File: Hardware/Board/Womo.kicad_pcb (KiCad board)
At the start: 4 copper layers, 255 x 150 mm, 464 parts, among them IC1 SPSGRFC-868, IC200 BTS6143D, IC201 BTS6143D, IC203 BTS6143D, IC204 BTS6143D, J1 USB_B_Micro, J2 Conn_ARM_JTAG_SWD_20, J3 SD_Card, J300 734-264, J301 733-368, J302 733-368, J303 733-368, J304 Truma, J305 Dormetic, J306 733-366, J307 733-366, J308 733-366, J309 733-366, J310 733-370, J311 734-163, J312 734-163, J313 734-163, J314 734-163, J315 734-168, J316 733-363, J317 RJ45_Shielded, J318 Spare, J319 SENSOR, J320 Raspberry_Pi_2_3, J321 Wasser, J322 Abwasser, J323 733-370, J324 Waveshare IoT Hat, J325 734-168, J326 733-366, J400 USB_B_Micro, J401 RJ45_Shielded, J500 SENSOR, K300 5-1393243-2, K301 5-1393243-2, K302 5-1393243-2, K303 5-1393243-2, Q100 2N7002, Q102 2N7002, Q103 2N7002, Q104 2N7002, Q200 2N7002, Q201 2N7002, Q202 2N7002, Q203 2N7002, SW1 Boot, SW3 Reset, U1 STM32L476ZGTx, U100 MAX17572, U101 MAX17572, U102 MAX17572, U104 MAX17574, U105 MAX17574, U2 M25Q128A, U200 SN74LV4052A, U201 TJA1029T, U202 TJA1029T, U203 TJA1029T, U204 TJA1029T, U205 SN74LV4052A, U206 SN74LV4052A, U207 MAX3072E, U208 MAX3072E, U209 MAX3072E, U210 MAX3072E, U211 MAX11615, U212 PCF8574A, U213 TJA1049T-3, U214 DS2482S-800+, U215 SN74LV4052A, U216 Si8642BB-B-IS1, U217 Si8642BB-B-IS1, U3 24AA02UID, U300 max4896atp+, U301 max4896atp+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

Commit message: Daten für Vortrag 36c3 ergänzt
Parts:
- moved J2 8.02 mm to (348.0, 169.5)
- moved R231 5.16 mm to (207.5, 141.2)
- moved R230 3.88 mm to (213.7, 141.2)
- moved FB212 2.45 mm to (211.7, 137.9)
- moved FB213 2.33 mm to (209.3, 137.9)
- moved D216 2.26 mm to (210.6, 141.5)
- moved C219 2.20 mm to (210.7, 145.1)
- moved C227 0.87 mm to (163.6, 244.4)
- moved J317 0.83 mm to (365.9, 266.8)
- moved J310 0.79 mm to (304.3, 266.4)
- moved J304 0.65 mm to (332.7, 142.1)
- moved J305 0.64 mm to (318.5, 139.3)
- moved J307 0.64 mm to (231.3, 133.5)
- moved J316 0.64 mm to (211.7, 133.5)
- moved J326 0.63 mm to (376.0, 133.5)
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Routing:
- net Net-(D218-Pad5): track 0.00 -> 21.6 mm
- net K4_NC: track 0.00 -> 18.7 mm
- net K2_NC: track 0.00 -> 17.7 mm
- net K3_NC: track 0.00 -> 17.7 mm
- net K1_NC: track 0.00 -> 17.7 mm
- net Net-(D216-Pad2): track 0.00 -> 16.0 mm, vias 0 -> 2
- net K2_COM: track 0.00 -> 15.8 mm
- net K3_COM: track 0.00 -> 15.7 mm
- net K1_COM: track 0.00 -> 15.3 mm
- net K4_COM: track 0.00 -> 15.0 mm
- net Net-(D216-Pad1): track 0.00 -> 12.9 mm
- net K1_NO: track 0.00 -> 12.2 mm
- net K2_NO: track 0.00 -> 10.8 mm
- net K3_NO: track 0.00 -> 10.8 mm
- net K4_NO: track 0.00 -> 10.5 mm
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- added copper zone on B.Cu, net DC_Input
- added copper zone on F.Cu, net HSS_1
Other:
- net class Medium added: clearance 0.2, trace_width 0.3, via_dia 0.8, via_drill 0.4
- net class Power_high added: clearance 0.2, trace_width 1.5, via_dia 0.8, via_drill 0.4
- net class Power_smal added: clearance 0.2, trace_width 0.5, via_dia 0.8, via_drill 0.4

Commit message: Kleinkram Layout
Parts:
- moved C221 5.02 mm to (177.3, 152.8)
- moved R310 4.92 mm to (346.8, 252.3), turned to 0 degrees
- moved R313 4.91 mm to (353.3, 252.3), turned to 180 degrees
- moved R312 3.34 mm to (351.6, 250.7), turned to 0 degrees
- moved R311 3.32 mm to (348.4, 250.7), turned to 180 degrees
- moved R317 3.03 mm to (354.1, 254.7)
- moved R315 2.82 mm to (349.1, 254.7)
- moved R316 2.80 mm to (350.8, 254.7)
- moved C325 2.69 mm to (346.8, 262.3), turned to 0 degrees
- moved R314 2.55 mm to (346.0, 254.7)
- moved C328 2.27 mm to (353.3, 262.3), turned to 180 degrees
- moved FB342 2.17 mm to (350.8, 257.9)
- moved FB341 2.15 mm to (349.1, 257.9)
- moved FB343 2.15 mm to (354.1, 257.9)
- moved FB340 2.12 mm to (346.0, 257.9)
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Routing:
- net GND: track 2.92 -> 86.1 mm, vias 15 -> 24
- net +3.3VA: track 0.00 -> 66.7 mm, vias 0 -> 6
- net Net-(D218-Pad1): track 1.75 -> 32.5 mm, vias 0 -> 2
- net Net-(D218-Pad3): track 1.74 -> 27.2 mm
- net Net-(D217-Pad1): track 1.71 -> 24.6 mm, vias 0 -> 3
- net Net-(D217-Pad5): track 1.74 -> 24.4 mm
- net Net-(D217-Pad4): track 1.74 -> 18.1 mm, vias 0 -> 2
- net Net-(D217-Pad3): track 1.74 -> 17.1 mm, vias 0 -> 2
- net Net-(C219-Pad1): track 0.00 -> 14.5 mm, vias 0 -> 2
- net Net-(D218-Pad4): track 8.57 -> 19.0 mm, vias 0 -> 2
- net Net-(C326-Pad1): track 0.00 -> 8.00 mm
- net Net-(C328-Pad1): track 0.00 -> 7.98 mm
- net Net-(C327-Pad1): track 0.00 -> 7.82 mm
- net Net-(C325-Pad1): track 0.00 -> 7.75 mm
- net AIN5: track 0.00 -> 3.26 mm
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
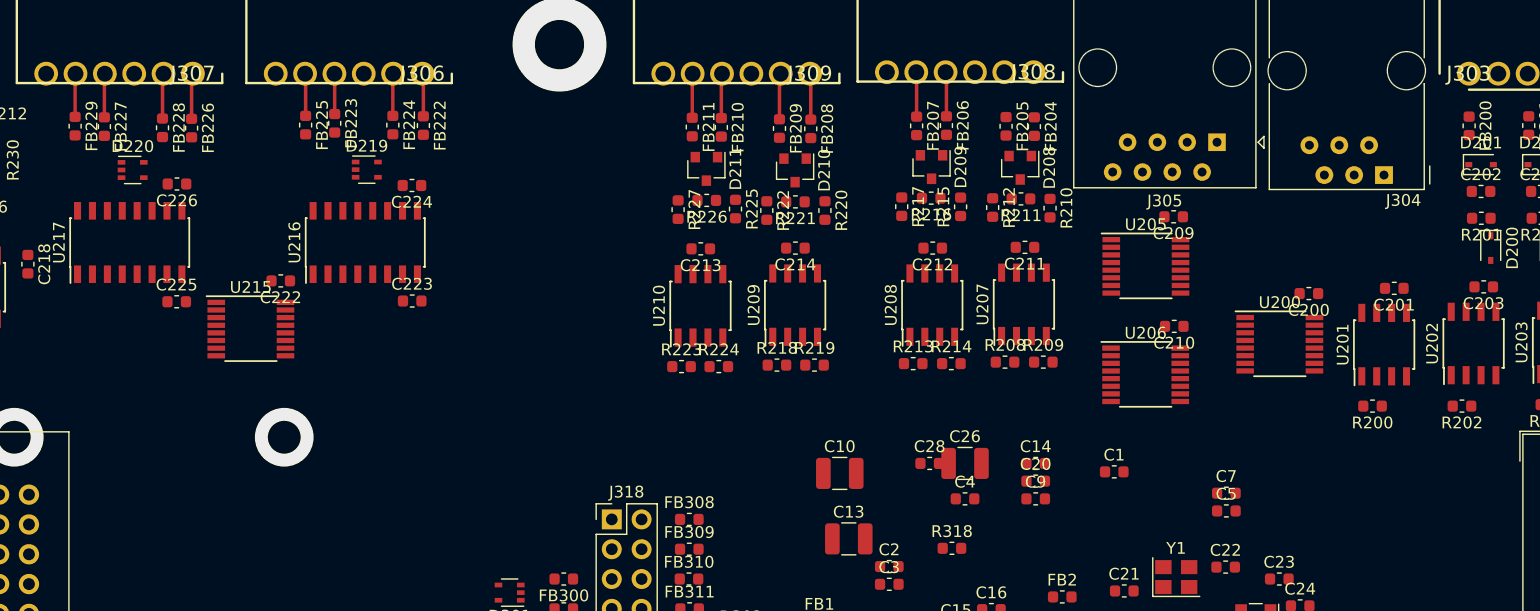
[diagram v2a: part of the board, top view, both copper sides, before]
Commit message: Layout Arbeit, Project Library sollte jetzt auf allen Rechnern funktionieren. Leerzeichen entfernt.
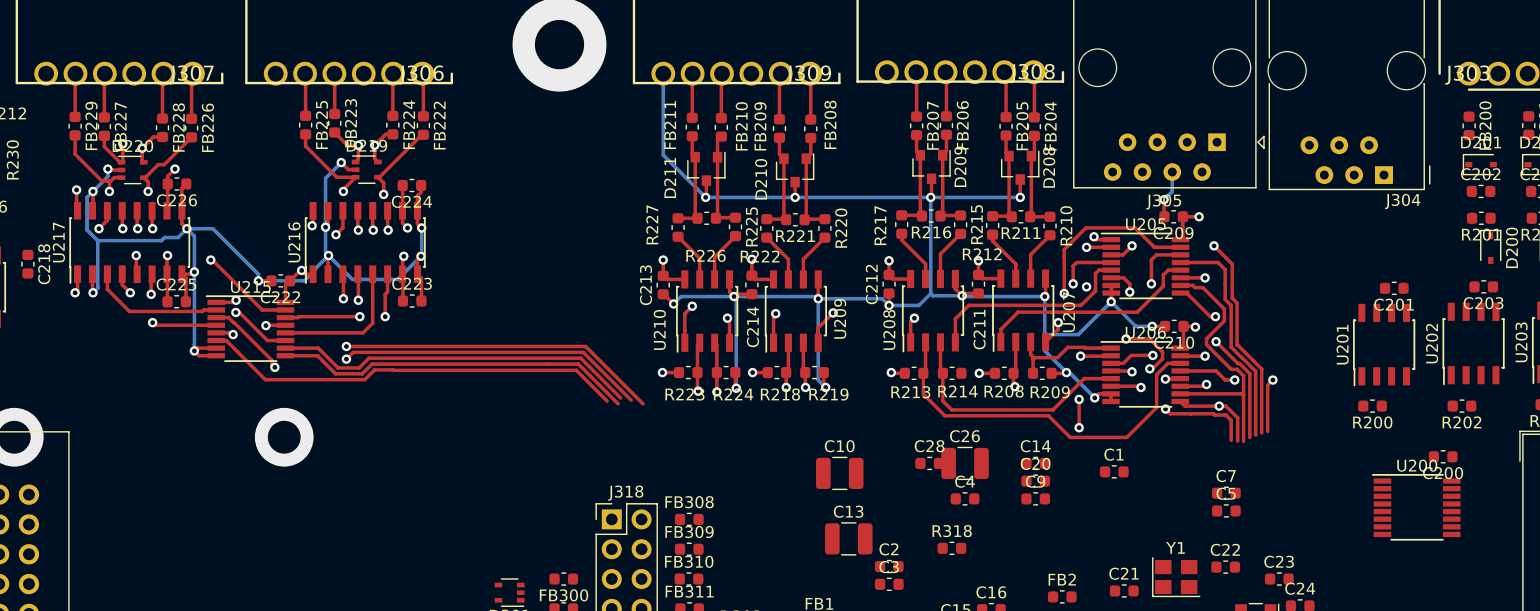
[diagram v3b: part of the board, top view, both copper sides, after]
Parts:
- moved U200 18.2 mm to (335.6, 170.5)
- moved C200 18.0 mm to (337.8, 166.1)
- moved C211 5.05 mm to (298.2, 151.4), turned to 90 degrees
- moved C214 4.86 mm to (278.9, 151.5), turned to 90 degrees
- moved C212 4.83 mm to (290.6, 151.4), turned to 90 degrees
- moved C213 4.45 mm to (271.3, 151.5), turned to 90 degrees
- moved R210 1.52 mm to (304.3, 146.5)
- moved R211 1.52 mm to (301.8, 145.7)
- moved R212 1.52 mm to (299.4, 146.4)
- moved R215 1.52 mm to (296.7, 146.3), turned to 270 degrees
- moved R216 1.52 mm to (294.2, 145.6)
- moved R217 1.52 mm to (291.7, 146.3)
- moved R220 1.52 mm to (285.1, 146.7)
- moved R221 1.52 mm to (282.6, 145.9)
- moved R222 1.52 mm to (280.2, 146.7)
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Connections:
- FB222 pad 2: Net-(D219-Pad1) -> Net-(D219-Pad4)
- FB223 pad 2: Net-(D219-Pad3) -> Net-(D219-Pad1)
- FB224 pad 2: Net-(D219-Pad4) -> Net-(D219-Pad5)
- FB225 pad 2: Net-(D219-Pad5) -> Net-(D219-Pad3)
- FB226 pad 2: Net-(D220-Pad1) -> Net-(D220-Pad4)
- FB227 pad 2: Net-(D220-Pad3) -> Net-(D220-Pad1)
- FB228 pad 2: Net-(D220-Pad4) -> Net-(D220-Pad5)
- FB229 pad 2: Net-(D220-Pad5) -> Net-(D220-Pad3)
- U205 pad 15: RX_RS485_2 -> RX_RS485_3
- U205 pad 3: LPUART3_TX_RS485 -> LPUART_TX_RS485
- U206 pad 1: TX_RS485_1 -> DE_RS485_1
- U206 pad 2: TX_RS485_3 -> DE_RS485_3
- U206 pad 4: TX_RS485_4 -> DE_RS485_4
- U206 pad 5: TX_RS485_2 -> DE_RS485_2
- U216 pad 11: Net-(D219-Pad5) -> Net-(D219-Pad3)
- U216 pad 12: Net-(D219-Pad4) -> Net-(D219-Pad5)
- U216 pad 13: Net-(D219-Pad3) -> Net-(D219-Pad1)
- U216 pad 14: Net-(D219-Pad1) -> Net-(D219-Pad4)
- U217 pad 11: Net-(D220-Pad5) -> Net-(D220-Pad3)
- U217 pad 12: Net-(D220-Pad4) -> Net-(D220-Pad5)
- U217 pad 13: Net-(D220-Pad3) -> Net-(D220-Pad1)
- U217 pad 14: Net-(D220-Pad1) -> Net-(D220-Pad4)
- U217 pad 4: TX_SER4 -> TX_SER_4
- U217 pad 5: RX_SER3 -> RX_SER_3
- U217 pad 6: RX_SER4 -> RX_SER_4
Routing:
- net +3.3VA: track 66.7 -> 319.8 mm, vias 6 -> 24
- net GND: track 86.1 -> 329.9 mm, vias 24 -> 53
- net RE_RS485_4: track 0.00 -> 52.0 mm, vias 0 -> 2
- net RX_RS485_4: track 0.00 -> 50.5 mm, vias 0 -> 2
- net RE_RS485_3: track 0.00 -> 50.5 mm, vias 0 -> 4
- net DE_RS485_4: track 0.00 -> 45.4 mm, vias 0 -> 2
- net RX_RS485_3: track 0.00 -> 44.2 mm, vias 0 -> 2
- net USART3_TX_SER: track 0.00 -> 39.5 mm, vias 0 -> 2
- net TX_RS485_4: track 0.00 -> 38.0 mm, vias 0 -> 2
- net USART3_RX_SER: track 0.00 -> 36.6 mm, vias 0 -> 2
- net SER_SEL_EN: track 0.00 -> 36.1 mm
- net DE_RS485_3: track 0.00 -> 33.2 mm, vias 0 -> 2
- net RE_RS485_2: track 0.00 -> 32.2 mm
- net TX_RS485_3: track 0.00 -> 31.4 mm, vias 0 -> 3
- net SER_SEL_A0: track 0.00 -> 31.0 mm
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
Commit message: Zwischenstand Layout, etliche Fehler im Schaltplan gefixt.
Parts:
- added D307: SP0504BAJT, Package_TO_SOT_SMD:SOT-353_SC-70-5, F.Cu at (367.7, 143.0)
- moved C305 118.1 mm to (339.0, 222.5), turned to 180 degrees
- moved U302 106.6 mm to (331.4, 227.6), turned to 270 degrees
- moved C304 97.9 mm to (327.6, 231.3), turned to 270 degrees
- moved C316 92.7 mm to (343.1, 231.4), turned to 270 degrees
- moved IC1 86.1 mm to (251.8, 208.6)
- moved U304 82.0 mm to (346.9, 227.6), turned to 270 degrees
- moved C317 80.7 mm to (346.9, 222.6), turned to 180 degrees
- moved R318 64.5 mm to (263.2, 229.5), turned to 90 degrees
- moved C29 47.9 mm to (331.3, 222.5), turned to 180 degrees
- moved C31 42.8 mm to (335.3, 231.2), turned to 270 degrees
- moved Q203 35.0 mm to (194.4, 233.7), turned to 270 degrees
- moved U6 33.9 mm to (339.1, 227.6)
- moved R250 31.3 mm to (195.4, 230.2), turned to 90 degrees
- moved R252 29.6 mm to (193.5, 230.2), turned to 270 degrees
- moved D305 25.8 mm to (285.1, 239.1), turned to 180 degrees
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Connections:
- C202 pad 1: Net-(C202-Pad1) -> LIN1
- C204 pad 1: Net-(C204-Pad1) -> LIN2
- C206 pad 1: Net-(C206-Pad1) -> LIN3
- C208 pad 1: Net-(C208-Pad1) -> LIN4
- D201 pad 1: Net-(C202-Pad1) -> Net-(D201-Pad1)
- D203 pad 1: Net-(C204-Pad1) -> Net-(D203-Pad1)
- D205 pad 1: Net-(C206-Pad1) -> Net-(D205-Pad1)
- D207 pad 1: Net-(C208-Pad1) -> Net-(D207-Pad1)
- D305 pad 3: I2C1_SDA -> Net-(D305-Pad3)
- D305 pad 4: I2C1_SCL -> Net-(D305-Pad4)
- D305 pad 5: +3.3VA -> Net-(D305-Pad5)
- FB200 pad 2: Net-(C202-Pad1) -> Net-(D201-Pad1)
- FB201 pad 2: Net-(C204-Pad1) -> Net-(D203-Pad1)
- FB202 pad 2: Net-(C206-Pad1) -> Net-(D205-Pad1)
- FB203 pad 2: Net-(C208-Pad1) -> Net-(D207-Pad1)
- J311 pad 1: K1_COM -> K1_NO
- J311 pad 2: K1_NC -> K1_COM
- J311 pad 3: K1_NO -> K1_NC
- J312 pad 1: K2_COM -> K2_NO
- J312 pad 2: K2_NC -> K2_COM
- J312 pad 3: K2_NO -> K2_NC
- J313 pad 1: K3_COM -> K3_NO
- J313 pad 2: K3_NC -> K3_COM
- J313 pad 3: K3_NO -> K3_NC
- J314 pad 1: K4_COM -> K4_NO
- J314 pad 2: K4_NC -> K4_COM
- J314 pad 3: K4_NO -> K4_NC
- R201 pad 2: Net-(C202-Pad1) -> Net-(D201-Pad1)
- R203 pad 2: Net-(C204-Pad1) -> Net-(D203-Pad1)
- R205 pad 2: Net-(C206-Pad1) -> Net-(D205-Pad1)
- R207 pad 2: Net-(C208-Pad1) -> Net-(D207-Pad1)
- U200 pad 13: UART4_RX_LIN -> USART2_RX_LIN
- U200 pad 3: UART4_TX_LIN -> USART2_TX_LIN
- U201 pad 6: Net-(C202-Pad1) -> Net-(D201-Pad1)
- U202 pad 6: Net-(C204-Pad1) -> Net-(D203-Pad1)
- U203 pad 6: Net-(C206-Pad1) -> Net-(D205-Pad1)
- U204 pad 6: Net-(C208-Pad1) -> Net-(D207-Pad1)
- U205 pad 3: LPUART_TX_RS485 -> LPUART3_TX_RS485
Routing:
- net GND: track 329.9 -> 943.7 mm, vias 53 -> 99
- net I2C2_SCL: track 0.00 -> 99.4 mm
- net I2C2_SDA: track 0.00 -> 98.4 mm
- net HSS_1_EN: track 0.00 -> 83.7 mm
- net HSS_2_EN: track 0.00 -> 80.0 mm
- net +5V: track 0.00 -> 78.3 mm, vias 0 -> 1
- net HSS_3_EN: track 0.00 -> 78.1 mm
- net K1_STATUS: track 0.00 -> 76.9 mm, vias 0 -> 1
- net HSS_4_EN: track 0.00 -> 73.7 mm
- net +3V3: track 0.00 -> 69.1 mm, vias 0 -> 5
- net +3.3VA: track 319.8 -> 388.5 mm, vias 24 -> 29
- net K2_STATUS: track 0.00 -> 65.4 mm, vias 0 -> 1
- net K1_RESET: track 0.00 -> 65.0 mm, vias 0 -> 2
- net I2C1_SDA: track 0.00 -> 61.4 mm
- net STB-CAN: track 0.00 -> 61.1 mm
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
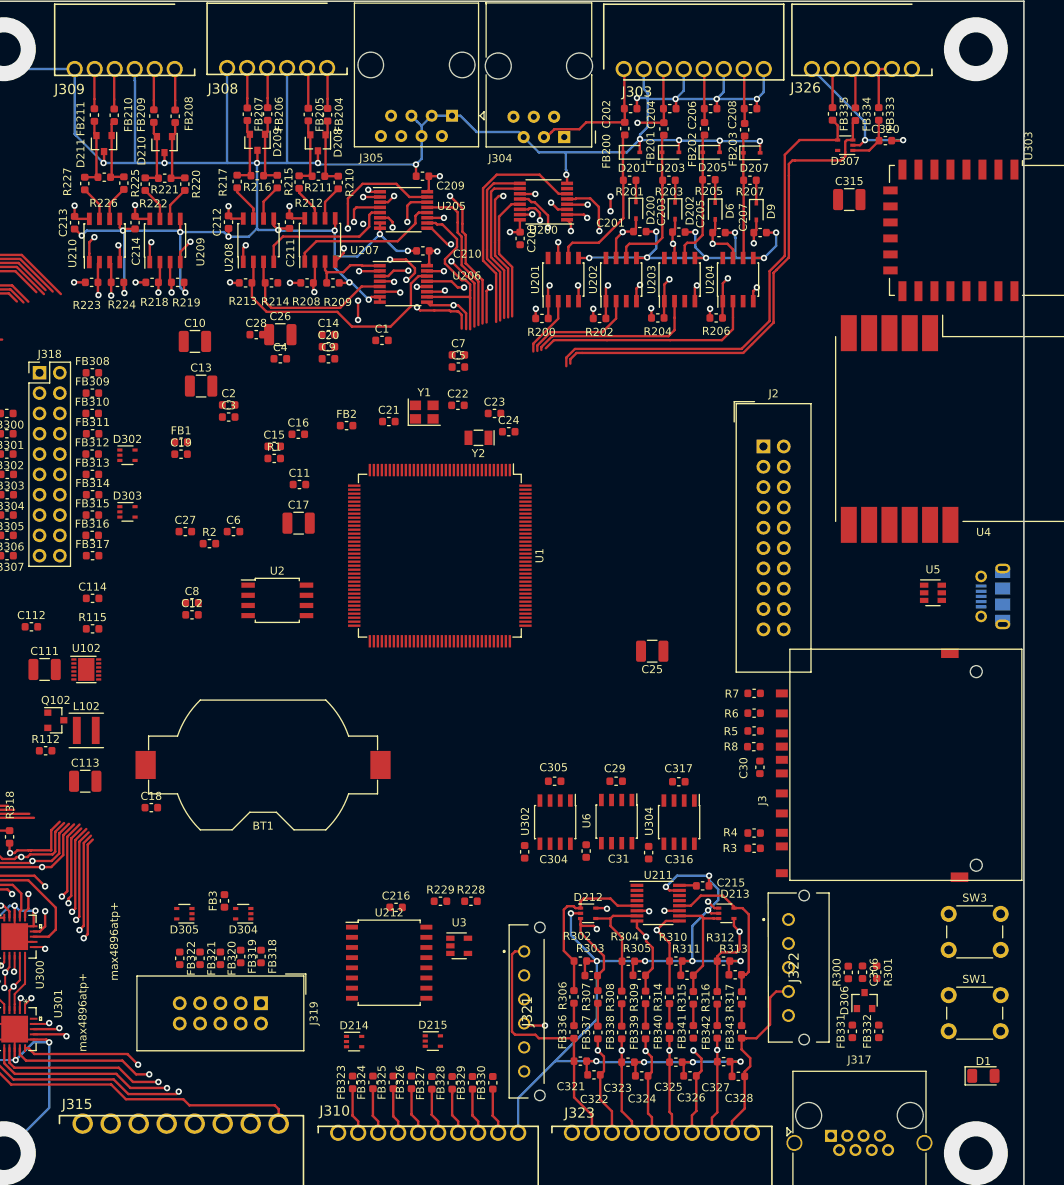
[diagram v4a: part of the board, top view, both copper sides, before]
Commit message: Fehlende Masse Abblockung CPU, Anfang Prozessor Routing
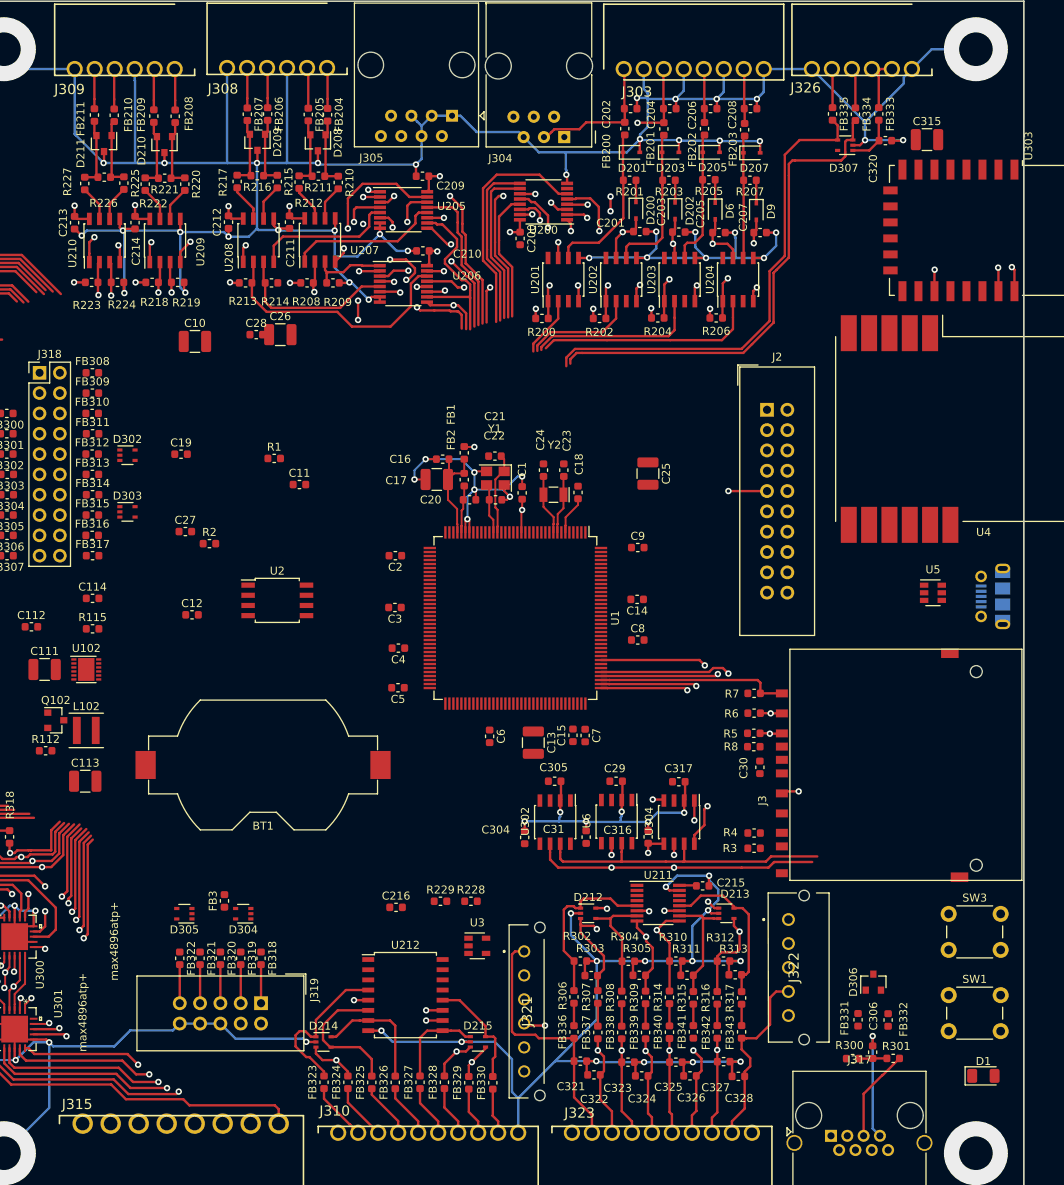
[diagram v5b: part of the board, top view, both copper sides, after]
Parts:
- moved C18 66.3 mm to (334.3, 186.4), turned to 90 degrees
- moved C13 60.9 mm to (328.7, 217.7), turned to 270 degrees
- moved C8 55.9 mm to (341.7, 204.9)
- moved C15 52.0 mm to (333.6, 216.8), turned to 90 degrees
- moved C14 50.8 mm to (341.7, 199.8), turned to 180 degrees
- moved C7 50.1 mm to (335.2, 216.8), turned to 270 degrees
- moved C9 45.3 mm to (341.7, 193.3)
- moved C6 41.0 mm to (323.2, 216.9), turned to 270 degrees
- moved C5 40.8 mm to (311.8, 210.8), turned to 180 degrees
- moved C4 39.1 mm to (311.8, 205.9), turned to 180 degrees
- moved FB1 35.7 mm to (320.0, 184.8), turned to 270 degrees
- moved C3 31.6 mm to (311.4, 200.8), turned to 180 degrees
- moved C2 28.1 mm to (311.4, 194.3), turned to 180 degrees
- moved C20 26.0 mm to (320.7, 187.3)
- moved C1 25.9 mm to (327.3, 186.5), turned to 90 degrees
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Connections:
- C1 pad 2: Net-(C1-Pad2) -> GND
- C13 pad 2: Net-(C13-Pad2) -> GND
- C14 pad 1: Net-(C13-Pad2) -> GND
- C15 pad 1: Net-(C13-Pad2) -> GND
- C16 pad 1: Net-(C13-Pad2) -> GND
- C17 pad 1: Net-(C13-Pad2) -> GND
- C2 pad 2: Net-(C1-Pad2) -> GND
- C3 pad 2: Net-(C1-Pad2) -> GND
- C305 pad 2: +5VD -> +5V
- C4 pad 2: Net-(C1-Pad2) -> GND
- C5 pad 2: Net-(C1-Pad2) -> GND
- C6 pad 2: Net-(C1-Pad2) -> GND
- C7 pad 2: Net-(C1-Pad2) -> GND
- C8 pad 2: Net-(C1-Pad2) -> GND
- C9 pad 2: Net-(C1-Pad2) -> GND
- R300 pad 1: CTRL_H -> CTRL_BUS_H
- R301 pad 2: CTRL_L -> CTRL_BUS_L
- U302 pad 3: +5VD -> +5V
- Y1 pad 2: GND1 -> GND
- Y1 pad 4: GND1 -> GND
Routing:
- net GND: track 943.7 -> 1119.4 mm, vias 99 -> 116
- net Net-(U303-Pad17): track 0.00 -> 109.6 mm, vias 0 -> 2
- net Net-(U303-Pad21): track 0.00 -> 107.9 mm, vias 0 -> 2
- net Net-(U303-Pad22): track 0.00 -> 103.9 mm, vias 0 -> 2
- net JTAG_TDI: track 0.00 -> 45.1 mm, vias 0 -> 1
- net JTAG_TCK: track 0.00 -> 43.2 mm, vias 0 -> 2
- net CTRL_L: track 0.00 -> 42.0 mm, vias 0 -> 4
- net CTRL_H: track 0.00 -> 39.0 mm
- net uSD_CLK: track 0.00 -> 38.2 mm, vias 0 -> 2
- net uSD_CMD: track 0.00 -> 28.0 mm, vias 0 -> 2
- net uSD_D3: track 0.00 -> 26.0 mm, vias 0 -> 2
- net uSD_D2: track 0.00 -> 24.1 mm
- net P0: track 0.00 -> 20.0 mm
- net P6: track 0.00 -> 18.6 mm, vias 0 -> 2
- net P2: track 0.00 -> 17.5 mm
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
